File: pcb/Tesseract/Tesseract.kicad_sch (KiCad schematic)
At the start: 27 parts, among them IC1 MAX98357AETE+T, J1 NHD-1.91-176176UBC3 Conn-1, J2 USB C Power Connector, J3 Speaker Connector, J4 RPI Power Connector, J5 LED Strip Connector, J6 RPI Signal Connector 1, J7 RPI Signal Connector 2, J8 NHD-1.91-176176UBC3 Conn-2, SW1 SW_Push, SW2 SW_Push, SW3 SW_Push, SW4 SW_Push

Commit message: Log work from a couple of days ago in journal
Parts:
- J4: footprint Connector_JST:JST_XH_B2B-XH-A_1x02_P2.50mm_Vertical -> Connector_JST:JST_XH_B3B-XH-A_1x03_P2.50mm_Vertical; symbol Connector:Conn_01x02_Socket -> Connector:Conn_01x03_Socket
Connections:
- net +3V3: now also J4.2 (Pin_2)
- net GND: now also J4.3 (Pin_3); no longer J4.2 (Pin_2)

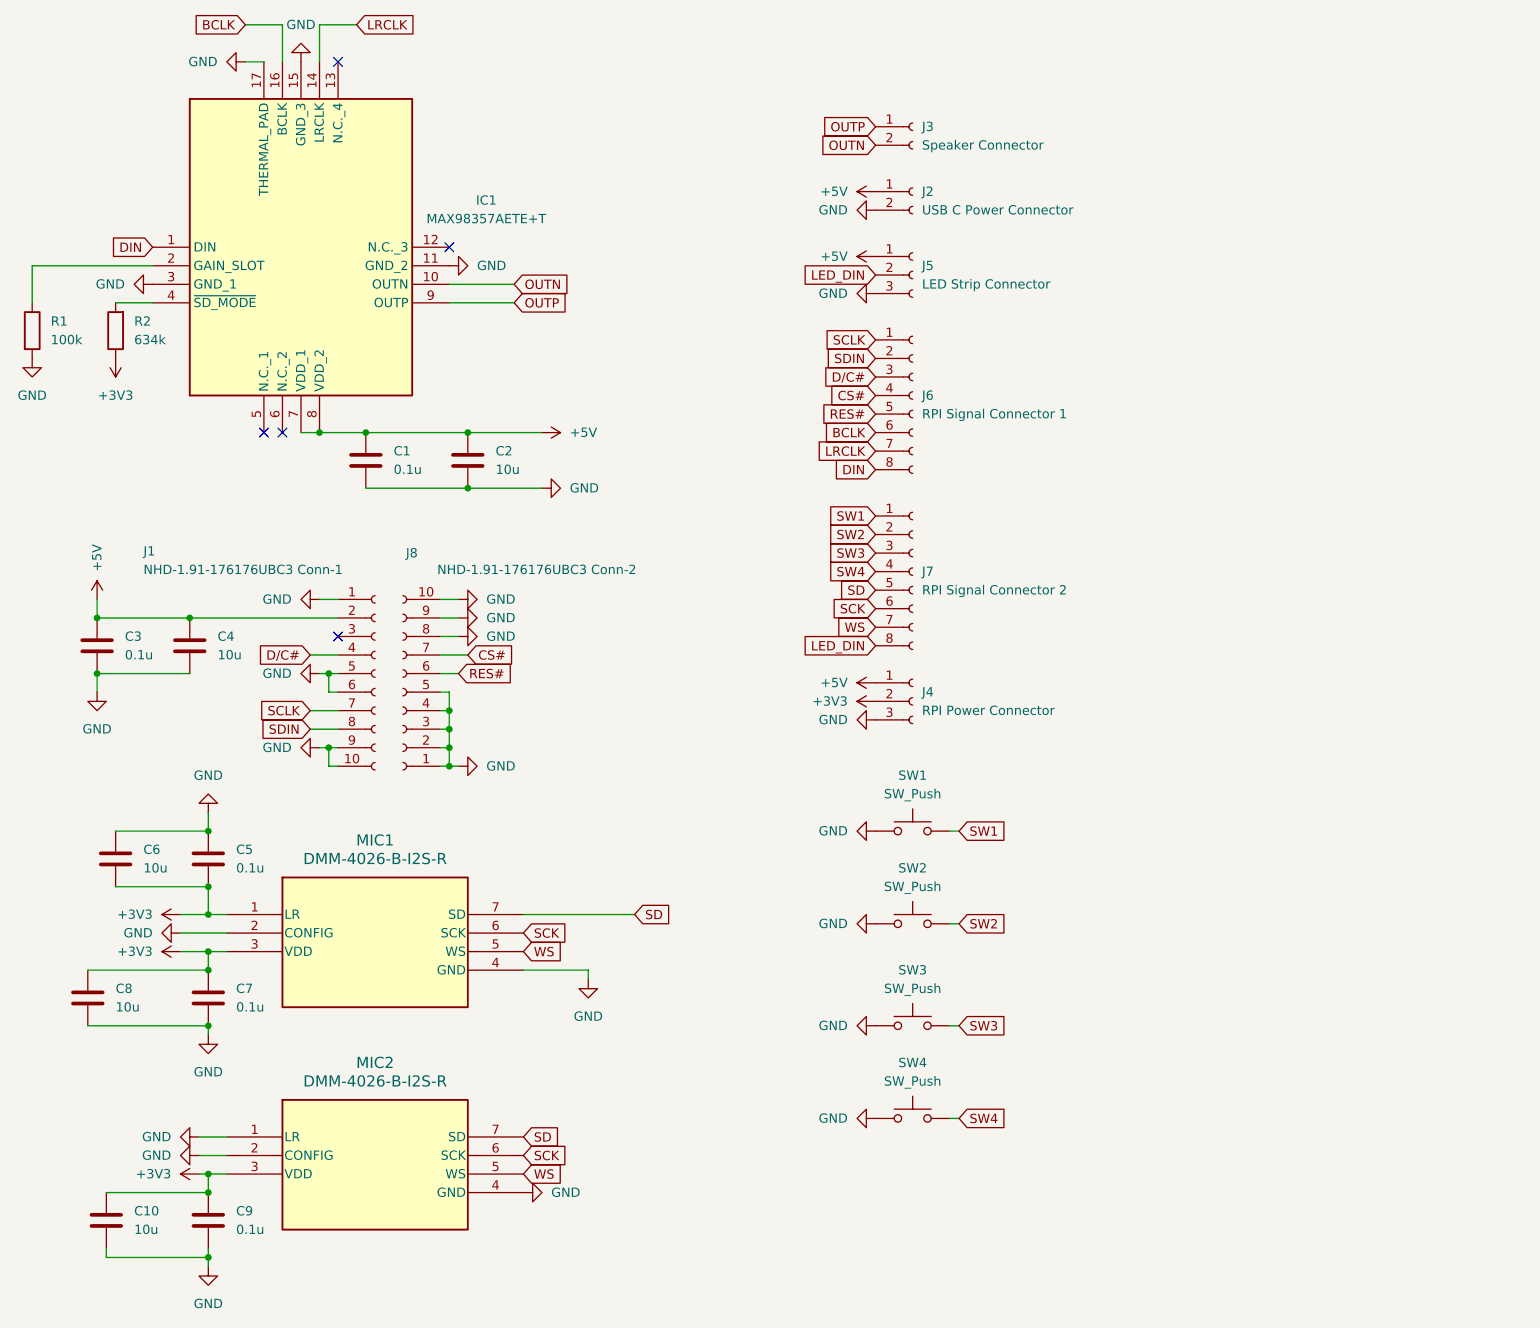
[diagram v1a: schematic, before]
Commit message: Remove top mic from PCB and schematic
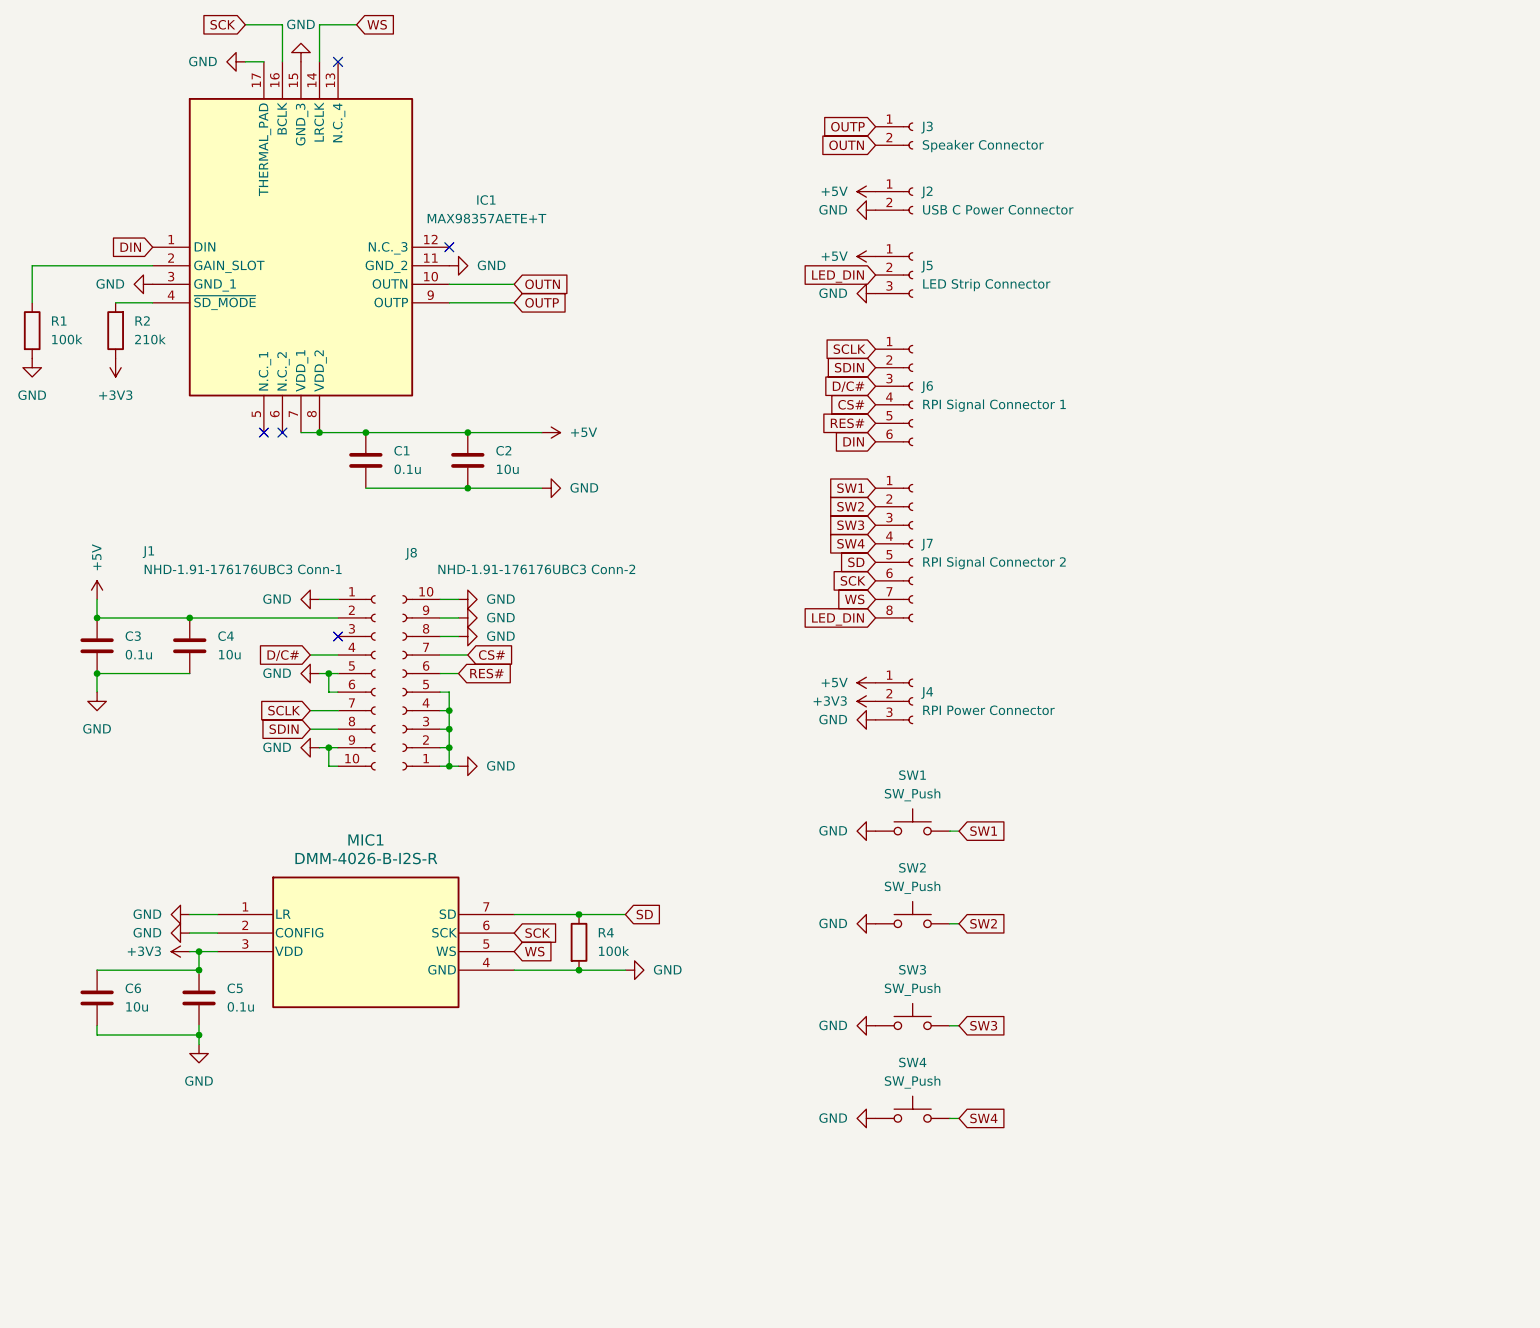
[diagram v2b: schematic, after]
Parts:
- removed C5, C7: 0.1u, Capacitor_SMD:C_0805_2012Metric_Pad1.18x1.45mm_HandSolder, symbol Device:C
- removed C6, C8: 10u, Capacitor_SMD:C_0805_2012Metric_Pad1.18x1.45mm_HandSolder, symbol Device:C
- removed MIC1: DMM-4026-B-I2S-R, Project Footprints:MIC_DMM-4026-B-I2S-R_PUI, symbol DMM-4026-B-I2S-R:DMM-4026-B-I2S-R
- added R4: 100k, Resistor_SMD:R_0805_2012Metric_Pad1.20x1.40mm_HandSolder, symbol Device:R
- J6: footprint Connector_JST:JST_XH_B8B-XH-A_1x08_P2.50mm_Vertical -> Connector_JST:JST_XH_B6B-XH-A_1x06_P2.50mm_Vertical; symbol Connector:Conn_01x08_Socket -> Connector:Conn_01x06_Socket
- R2: value 634k -> 210k
- renumbered C9 to C5, C10 to C6, MIC2 to MIC1
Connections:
- net DIN: now also J6.6 (Pin_6); no longer J6.8 (Pin_8)
- net GND: now also R4.2
- net SCK: now also IC1.16 (BCLK)
- net SD: now also R4.1
- net WS: now also IC1.14 (LRCLK)
- removed net BCLK: IC1.16 (BCLK), J6.6 (Pin_6)
- removed net LRCLK: IC1.14 (LRCLK), J6.7 (Pin_7)
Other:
- moved on the sheet: C5, C6, J7, MIC1

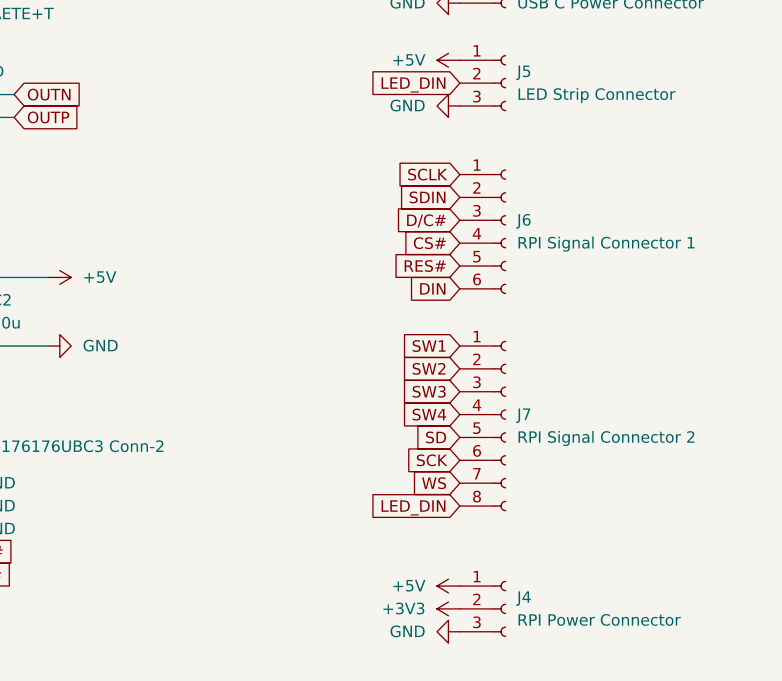
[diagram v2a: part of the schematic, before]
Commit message: Change PCB and schematic connectors for easier wiring
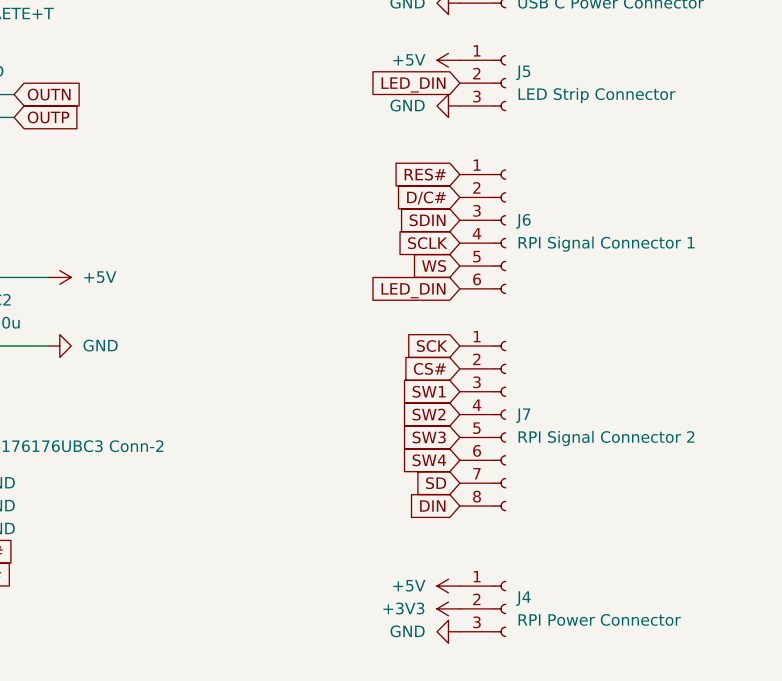
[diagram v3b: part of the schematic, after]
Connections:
- net CS#: now also J7.2 (Pin_2); no longer J6.4 (Pin_4)
- net DIN: now also J7.8 (Pin_8); no longer J6.6 (Pin_6)
- net D/C#: now also J6.2 (Pin_2); no longer J6.3 (Pin_3)
- net LED_DIN: now also J6.6 (Pin_6); no longer J7.8 (Pin_8)
- net RES#: now also J6.1 (Pin_1); no longer J6.5 (Pin_5)
- net SCK: now also J7.1 (Pin_1); no longer J7.6 (Pin_6)
- net SCLK: now also J6.4 (Pin_4); no longer J6.1 (Pin_1)
- net SD: now also J7.7 (Pin_7); no longer J7.5 (Pin_5)
- net SDIN: now also J6.3 (Pin_3); no longer J6.2 (Pin_2)
- net SW1: now also J7.3 (Pin_3); no longer J7.1 (Pin_1)
- net SW2: now also J7.4 (Pin_4); no longer J7.2 (Pin_2)
- net SW3: now also J7.5 (Pin_5); no longer J7.3 (Pin_3)
- net SW4: now also J7.6 (Pin_6); no longer J7.4 (Pin_4)
- net WS: now also J6.5 (Pin_5); no longer J7.7 (Pin_7)

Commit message: Update PCB and schematic related files
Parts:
- J6: footprint Connector_JST:JST_XH_B6B-XH-A_1x06_P2.50mm_Vertical -> Connector_JST:JST_XH_B7B-XH-A_1x07_P2.50mm_Vertical; symbol Connector:Conn_01x06_Socket -> Connector:Conn_01x07_Socket
- J7: footprint Connector_JST:JST_XH_B8B-XH-A_1x08_P2.50mm_Vertical -> Connector_JST:JST_XH_B7B-XH-A_1x07_P2.50mm_Vertical; symbol Connector:Conn_01x08_Socket -> Connector:Conn_01x07_Socket
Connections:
- net DIN: now also J6.1 (Pin_1); no longer J7.8 (Pin_8)
- net D/C#: now also J6.3 (Pin_3); no longer J6.2 (Pin_2)
- net LED_DIN: now also J6.7 (Pin_7); no longer J6.6 (Pin_6)
- net RES#: now also J6.2 (Pin_2); no longer J6.1 (Pin_1)
- net SCLK: now also J6.5 (Pin_5); no longer J6.4 (Pin_4)
- net SDIN: now also J6.4 (Pin_4); no longer J6.3 (Pin_3)
- net WS: now also J6.6 (Pin_6); no longer J6.5 (Pin_5)
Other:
- note added: "Main PCB Schematic"
- note added: "Tesseract v1.0 Schematic"
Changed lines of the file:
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@@
 	(generator_version "9.0")
 	(paper "A4")
+	(text "Main PCB Schematic"
+		(exclude_from_sim no)
+		(at 199.39 174.244 0)
+		(effects
+			(font
+				(size 2.5 2.5)
+				(thickness 0.3125)
+				(color 0 0 0 1)
+			)
+		)
+	)
+	(text "Tesseract v1.0 Schematic"
+		(exclude_from_sim no)
+		(at 198.882 189.738 0)
+		(effects
+			(font
+				(size 1.27 1.27)
+			)
+		)
+	)
 	(junction
 		(at 40.64 144.78)
@@
 	(global_label "DIN"
 		(shape input)
-		(at 133.35 99.06 180)
+		(at 133.35 59.69 180)
 		(fields_autoplaced yes)
 		(effects
@@
 		)
 		(property "Intersheetrefs" "${INTERSHEET_REFS}"
-			(at 127.1595 99.06 0)
+			(at 127.1595 59.69 0)
 			(effects
 				(font
@@
 	)
 	(symbol
-		(lib_id "Connector:Conn_01x08_Socket")
+		(lib_id "Connector:Conn_01x07_Socket")
 		(at 138.43 88.9 0)
 		(unit 1)
@@
 		(fields_autoplaced yes)
 		(property "Reference" "J7"
-			(at 139.7 88.8999 0)
+			(at 139.7 87.6299 0)
 			(effects
 				(font
@@
 		)
 		(property "Value" "RPI Signal Connector 2"
-			(at 139.7 91.4399 0)
+			(at 139.7 90.1699 0)
 			(effects
 				(font
@@
 			)
 		)
-		(property "Footprint" "Connector_JST:JST_XH_B8B-XH-A_1x08_P2.50mm_Vertical"
+		(property "Footprint" "Connector_JST:JST_XH_B7B-XH-A_1x07_P2.50mm_Vertical"
 			(at 138.43 88.9 0)
 			(effects
@@
 			)
 		)
-		(property "Description" "Generic connector, single row, 01x08, script generated"
+		(property "Description" "Generic connector, single row, 01x07, script generated"
 			(at 138.43 88.9 0)
 			(effects
@@
 		(pin "7"
 		)
-		(pin "8"
-		)
 		(pin "4"
 		)
@@
 	)
 	(symbol
-		(lib_id "Connector:Conn_01x06_Socket")
+		(lib_id "Connector:Conn_01x07_Socket")
 		(at 138.43 67.31 0)
 		(unit 1)
@@
 		(fields_autoplaced yes)
 		(property "Reference" "J6"
-			(at 139.7 67.3099 0)
+			(at 139.7 66.0399 0)
 			(effects
 				(font
@@
 		)
 		(property "Value" "RPI Signal Connector 1"
-			(at 139.7 69.8499 0)
+			(at 139.7 68.5799 0)
 			(effects
 				(font
@@
 			)
 		)
-		(property "Footprint" "Connector_JST:JST_XH_B6B-XH-A_1x06_P2.50mm_Vertical"
+		(property "Footprint" "Connector_JST:JST_XH_B7B-XH-A_1x07_P2.50mm_Vertical"
 			(at 138.43 67.31 0)
 			(effects
@@
 			)
 		)
-		(property "Description" "Generic connector, single row, 01x06, script generated"
+		(property "Description" "Generic connector, single row, 01x07, script generated"
 			(at 138.43 67.31 0)
 			(effects
@@
 		(pin "5"
 		)
+		(pin "7"
+		)
 		(instances
